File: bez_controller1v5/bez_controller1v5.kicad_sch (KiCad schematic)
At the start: 75 parts, among them J1 Conn_01x03_Male, J10 IMU Conn_01x03_Female, J11 Conn_01x03_Male, J12 Conn_01x03_Male, J13 USB_B_Mini, J2 Conn_01x03_Male, J3 Conn_01x03_Male, J4 Screw_Terminal_01x02, J5 Conn_01x03_Male, J6 Conn_01x03_Male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

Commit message: fixing some routing and components footprint
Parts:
- D2, D4: footprint LED_THT:LED_D5.0mm_Clear -> LED_SMD:LED_0603_1608Metric
- FB1, FB2: footprint Inductor_THT:L_Axial_L5.3mm_D2.2mm_P7.62mm_Horizontal_Vishay_IM-1 -> Inductor_SMD:L_0603_1608Metric
- R3: footprint Resistor_SMD:R_0603_1608Metric -> Resistor_SMD:R_0805_2012Metric
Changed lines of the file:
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@@
       (effects (font (size 1.27 1.27)) (justify right))
     )
-    (property "Footprint" "Inductor_THT:L_Axial_L5.3mm_D2.2mm_P7.62mm_Horizontal_Vishay_IM-1" (at 22.098 46.355 90)
+    (property "Footprint" "Inductor_SMD:L_0603_1608Metric" (at 22.098 46.355 90)
       (effects (font (size 1.27 1.27)) hide)
     )
@@
       (effects (font (size 1.27 1.27)))
     )
-    (property "Footprint" "Inductor_THT:L_Axial_L5.3mm_D2.2mm_P7.62mm_Horizontal_Vishay_IM-1" (at 168.275 90.678 90)
+    (property "Footprint" "Inductor_SMD:L_0603_1608Metric" (at 168.275 90.678 90)
       (effects (font (size 1.27 1.27)) hide)
     )
@@
       (effects (font (size 1.27 1.27)) (justify left))
     )
-    (property "Footprint" "Resistor_SMD:R_0603_1608Metric" (at 83.058 67.945 90)
+    (property "Footprint" "Resistor_SMD:R_0805_2012Metric" (at 83.058 67.945 90)
       (effects (font (size 1.27 1.27)) hide)
     )
@@
       (effects (font (size 1.27 1.27)) (justify right))
     )
-    (property "Footprint" "LED_THT:LED_D5.0mm_Clear" (at 109.855 34.925 0)
+    (property "Footprint" "LED_SMD:LED_0603_1608Metric" (at 109.855 34.925 0)
       (effects (font (size 1.27 1.27)) hide)
     )
@@
       (effects (font (size 1.27 1.27)))
     )
-    (property "Footprint" "LED_THT:LED_D5.0mm_Clear" (at 166.37 142.24 0)
-      (effects (font (size 1.27 1.27)) hide)
-    )
+    (property "Footprint" "LED_SMD:LED_0603_1608Metric" (at 166.37 142.24 0)
+      (effects (font (size 1.27 1.27)) hide)
+    )

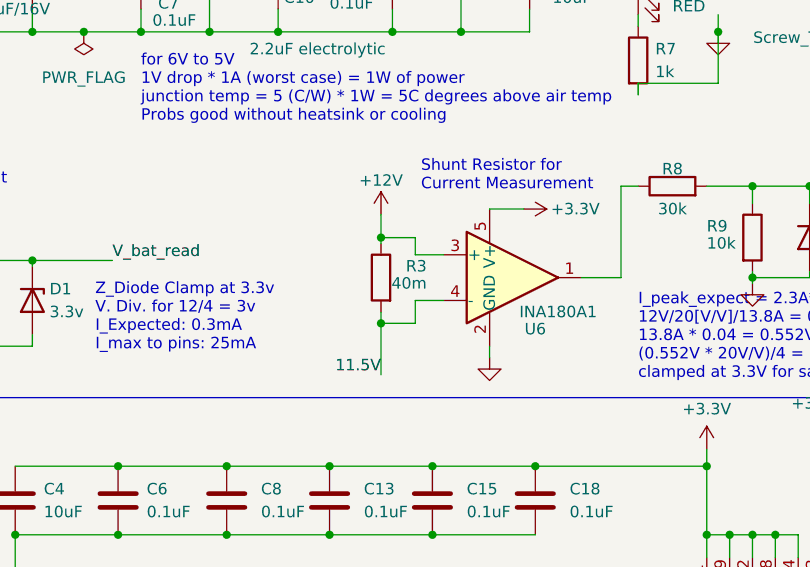
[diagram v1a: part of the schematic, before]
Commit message: change footprint of shunt R and electrolytic C
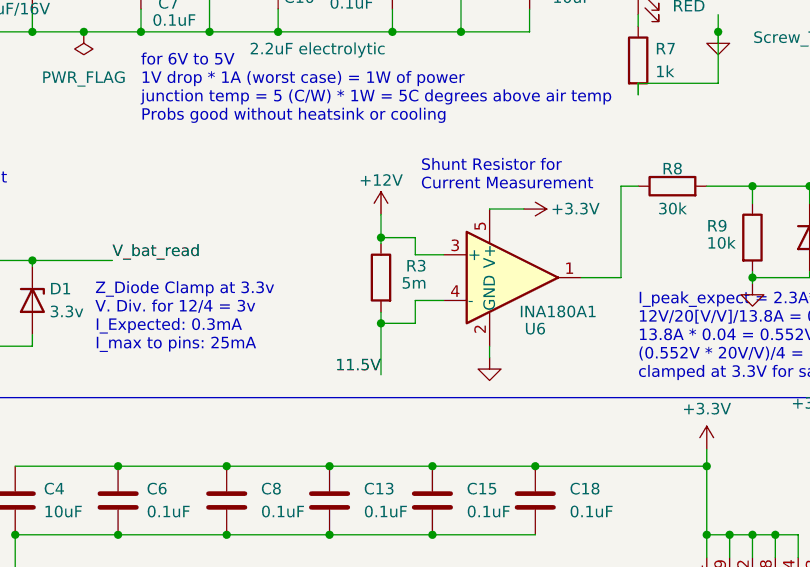
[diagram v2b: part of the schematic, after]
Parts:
- C10: footprint Capacitor_SMD:CP_Elec_4x5.4 -> Capacitor_THT:CP_Radial_D8.0mm_P3.50mm
- R3: value 40m -> 5m; footprint Resistor_SMD:R_0805_2012Metric -> Resistor_SMD:R_2010_5025Metric
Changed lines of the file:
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@@
       (effects (font (size 1.27 1.27)) (justify left))
     )
-    (property "Value" "40m" (at 86.36 68.58 0)
-      (effects (font (size 1.27 1.27)) (justify left))
-    )
-    (property "Footprint" "Resistor_SMD:R_0805_2012Metric" (at 83.058 67.945 90)
+    (property "Value" "5m" (at 86.36 68.58 0)
+      (effects (font (size 1.27 1.27)) (justify left))
+    )
+    (property "Footprint" "Resistor_SMD:R_2010_5025Metric" (at 83.058 67.945 90)
       (effects (font (size 1.27 1.27)) hide)
     )
@@
       (effects (font (size 1.27 1.27)) (justify left))
     )
-    (property "Footprint" "Capacitor_SMD:CP_Elec_4x5.4" (at 70.8152 38.1 0)
-      (effects (font (size 1.27 1.27)) hide)
-    )
+    (property "Footprint" "Capacitor_THT:CP_Radial_D8.0mm_P3.50mm" (at 70.8152 38.1 0)
+      (effects (font (size 1.27 1.27)) hide)
+    )

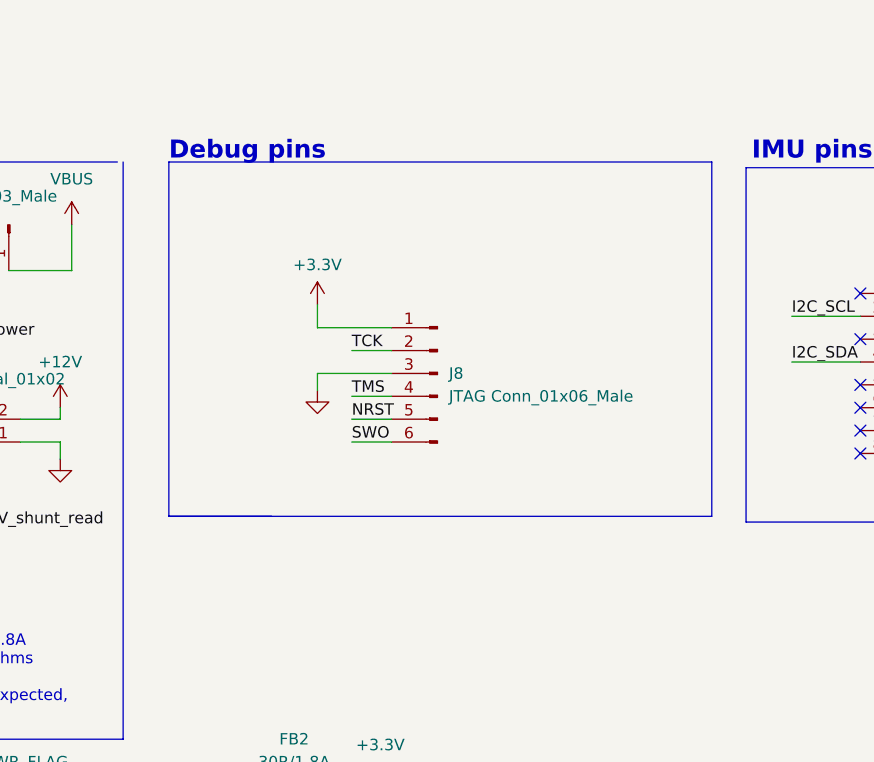
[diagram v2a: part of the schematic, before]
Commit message: add headers for GPIO/buttons
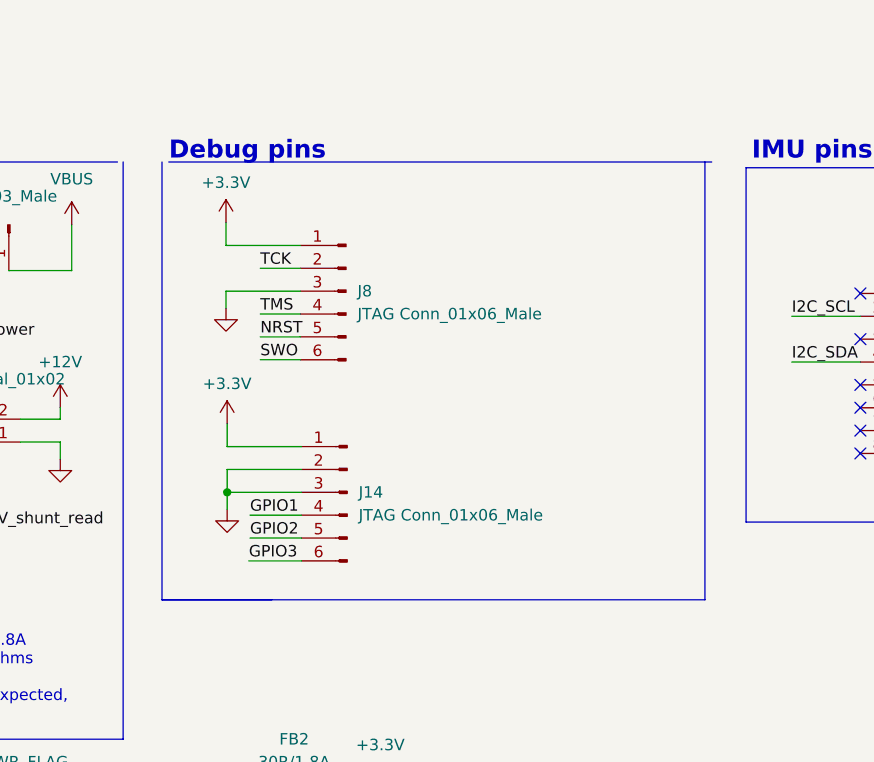
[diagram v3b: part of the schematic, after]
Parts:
- added J14: JTAG Conn_01x06_Male, Connector_PinHeader_2.54mm:PinHeader_1x06_P2.54mm_Vertical, symbol Connector:Conn_01x06_Male
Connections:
- net +3.3V: now also J14.1 (Pin_1)
- net GND: now also J14.2 (Pin_2), J14.3 (Pin_3)
- new net GPIO1: J14.4 (Pin_4)
- new net GPIO2: J14.5 (Pin_5)
- new net GPIO3: J14.6 (Pin_6)
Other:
- moved on the sheet: J8

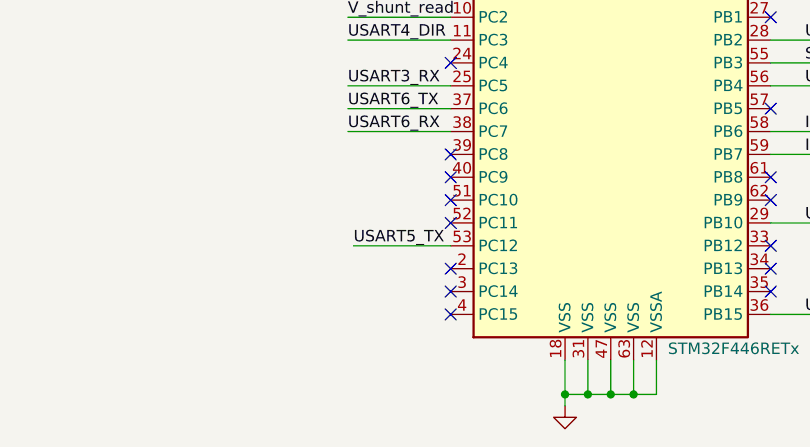
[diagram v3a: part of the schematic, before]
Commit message: routed IMU pins and minor changes
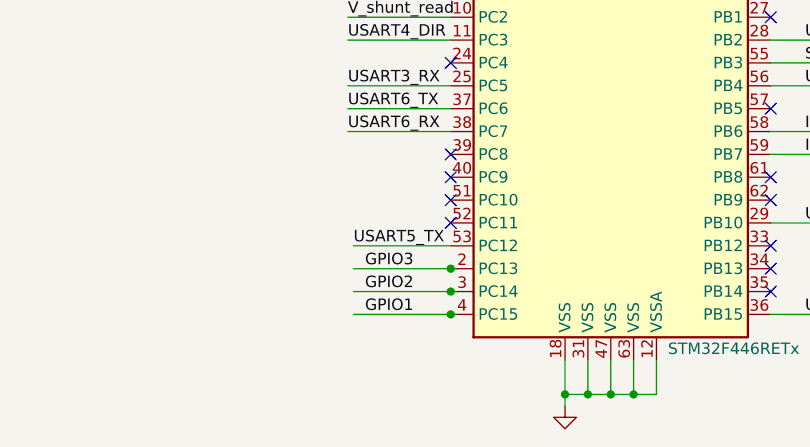
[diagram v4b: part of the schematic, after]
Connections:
- net GPIO1: now also U7.4 (PC15)
- net GPIO2: now also U7.3 (PC14)
- net GPIO3: now also U7.2 (PC13)
- no-connect marks 29 -> 26
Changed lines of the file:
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@@
   (junction (at 52.07 88.9) (diameter 0) (color 0 0 0 0)
   )
+  (junction (at 104.775 182.88) (diameter 0) (color 0 0 0 0)
+  )
   (junction (at 64.135 88.9) (diameter 0) (color 0 0 0 0)
   )
@@
   )
   (junction (at 133.35 -45.085) (diameter 0) (color 0 0 0 0)
+  )
+  (junction (at 104.775 180.34) (diameter 0) (color 0 0 0 0)
+  )
+  (junction (at 104.775 177.8) (diameter 0) (color 0 0 0 0)
   )
   (junction (at 81.28 73.025) (diameter 0) (color 0 0 0 0)
@@
   (no_connect (at 104.775 167.64))
   (no_connect (at 140.335 160.02))
-  (no_connect (at 104.775 180.34))
   (no_connect (at 104.775 165.1))
   (no_connect (at 140.335 177.8))
-  (no_connect (at 104.775 177.8))
   (no_connect (at 140.335 149.86))
   (no_connect (at 276.86 135.255))
@@
   (no_connect (at 140.335 147.32))
   (no_connect (at 231.14 31.75))
-  (no_connect (at 104.775 182.88))
   (no_connect (at 231.14 44.45))
   (no_connect (at 104.775 144.78))
@@
     (stroke (width 0) (type default))
   )
+  (wire (pts (xy 93.98 182.88) (xy 104.775 182.88))
+    (stroke (width 0) (type default))
+  )
   (wire (pts (xy 143.51 24.13) (xy 143.51 29.21))
     (stroke (width 0) (type default))
@@
     (stroke (width 0) (type default))
   )
+  (wire (pts (xy 93.98 180.34) (xy 104.775 180.34))
+    (stroke (width 0) (type default))
+  )
   (polyline (pts (xy 283.21 90.805) (xy 283.21 73.66))
     (stroke (width 0) (type default))
@@
     (stroke (width 0) (type default))
   )
+  (wire (pts (xy 104.775 177.8) (xy 105.41 177.8))
+    (stroke (width 0) (type default))
+  )
   (wire (pts (xy 54.61 40.64) (xy 62.23 40.64))
     (stroke (width 0) (type default))
@@
     (stroke (width 0) (type default))
   )
+  (wire (pts (xy 93.98 177.8) (xy 104.775 177.8))
+    (stroke (width 0) (type default))
+  )
   (wire (pts (xy 62.23 36.83) (xy 62.23 40.64))
     (stroke (width 0) (type default))
@@
     (stroke (width 0) (type default))
   )
+  (wire (pts (xy 104.775 182.88) (xy 105.41 182.88))
+    (stroke (width 0) (type default))
+  )
   (wire (pts (xy 164.465 39.116) (xy 168.91 39.116))
     (stroke (width 0) (type default))
@@
   )
   (wire (pts (xy 52.07 96.52) (xy 64.135 96.52))
+    (stroke (width 0) (type default))
+  )
+  (wire (pts (xy 104.775 180.34) (xy 105.41 180.34))
     (stroke (width 0) (type default))
   )
@@
     (effects (font (size 1.27 1.27)) (justify left bottom))
   )
+  (label "GPIO2" (at 95.25 180.34 0) (fields_autoplaced)
+    (effects (font (size 1.27 1.27)) (justify left bottom))
+  )
+  (label "GPIO1" (at 95.25 182.88 0) (fields_autoplaced)
+    (effects (font (size 1.27 1.27)) (justify left bottom))
+  )
   (label "NRST" (at 164.465 36.576 0) (fields_autoplaced)
     (effects (font (size 1.27 1.27)) (justify left bottom))
@@
     (effects (font (size 1.27 1.27)) (justify left bottom))
   )
+  (label "GPIO3" (at 95.25 177.8 0) (fields_autoplaced)
+    (effects (font (size 1.27 1.27)) (justify left bottom))
+  )

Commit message: added label for pins, changed USB and C10 footprint
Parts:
- C10: footprint Capacitor_THT:CP_Radial_D8.0mm_P3.50mm -> Capacitor_THT:CP_Radial_D5.0mm_P2.00mm
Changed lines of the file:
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@@
       (effects (font (size 1.27 1.27)) (justify left))
     )
-    (property "Footprint" "Capacitor_THT:CP_Radial_D8.0mm_P3.50mm" (at 70.8152 38.1 0)
+    (property "Footprint" "Capacitor_THT:CP_Radial_D5.0mm_P2.00mm" (at 70.8152 38.1 0)
       (effects (font (size 1.27 1.27)) hide)
     )

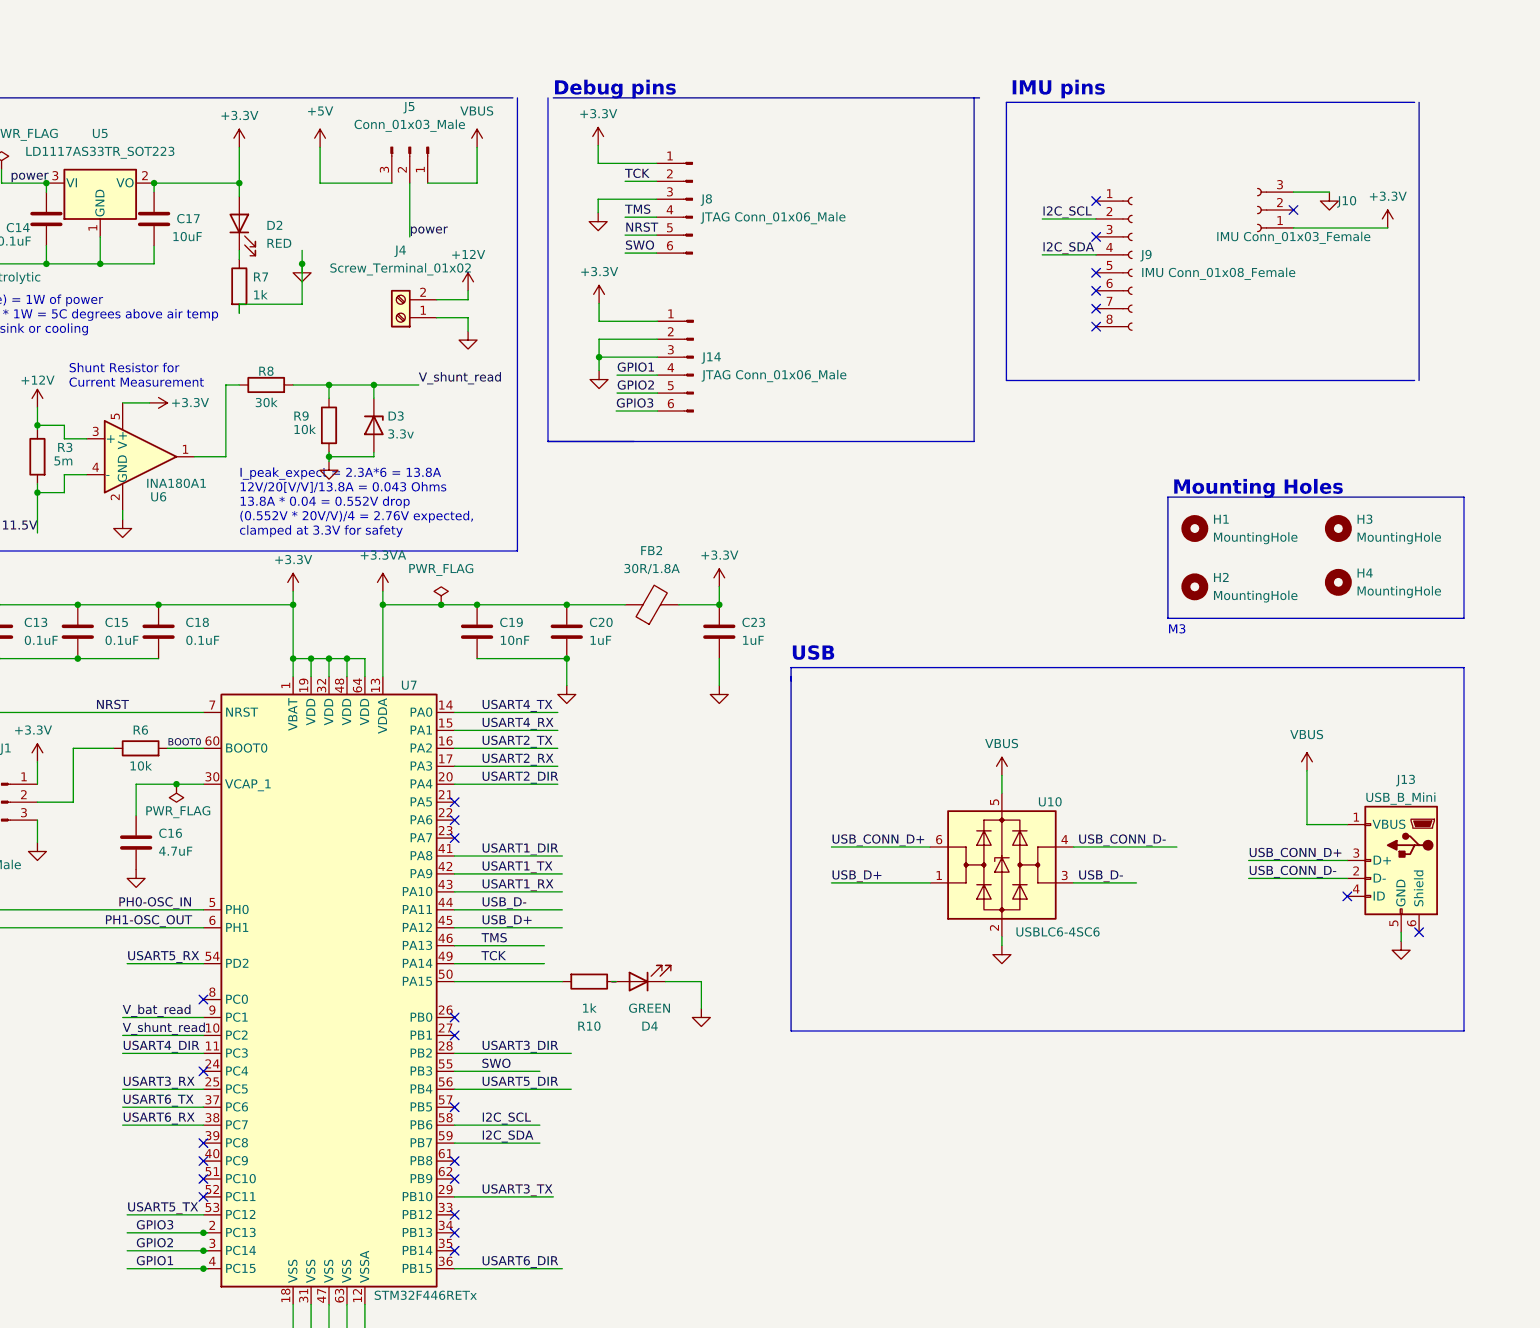
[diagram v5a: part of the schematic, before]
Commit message: Add SPI lines for IMU
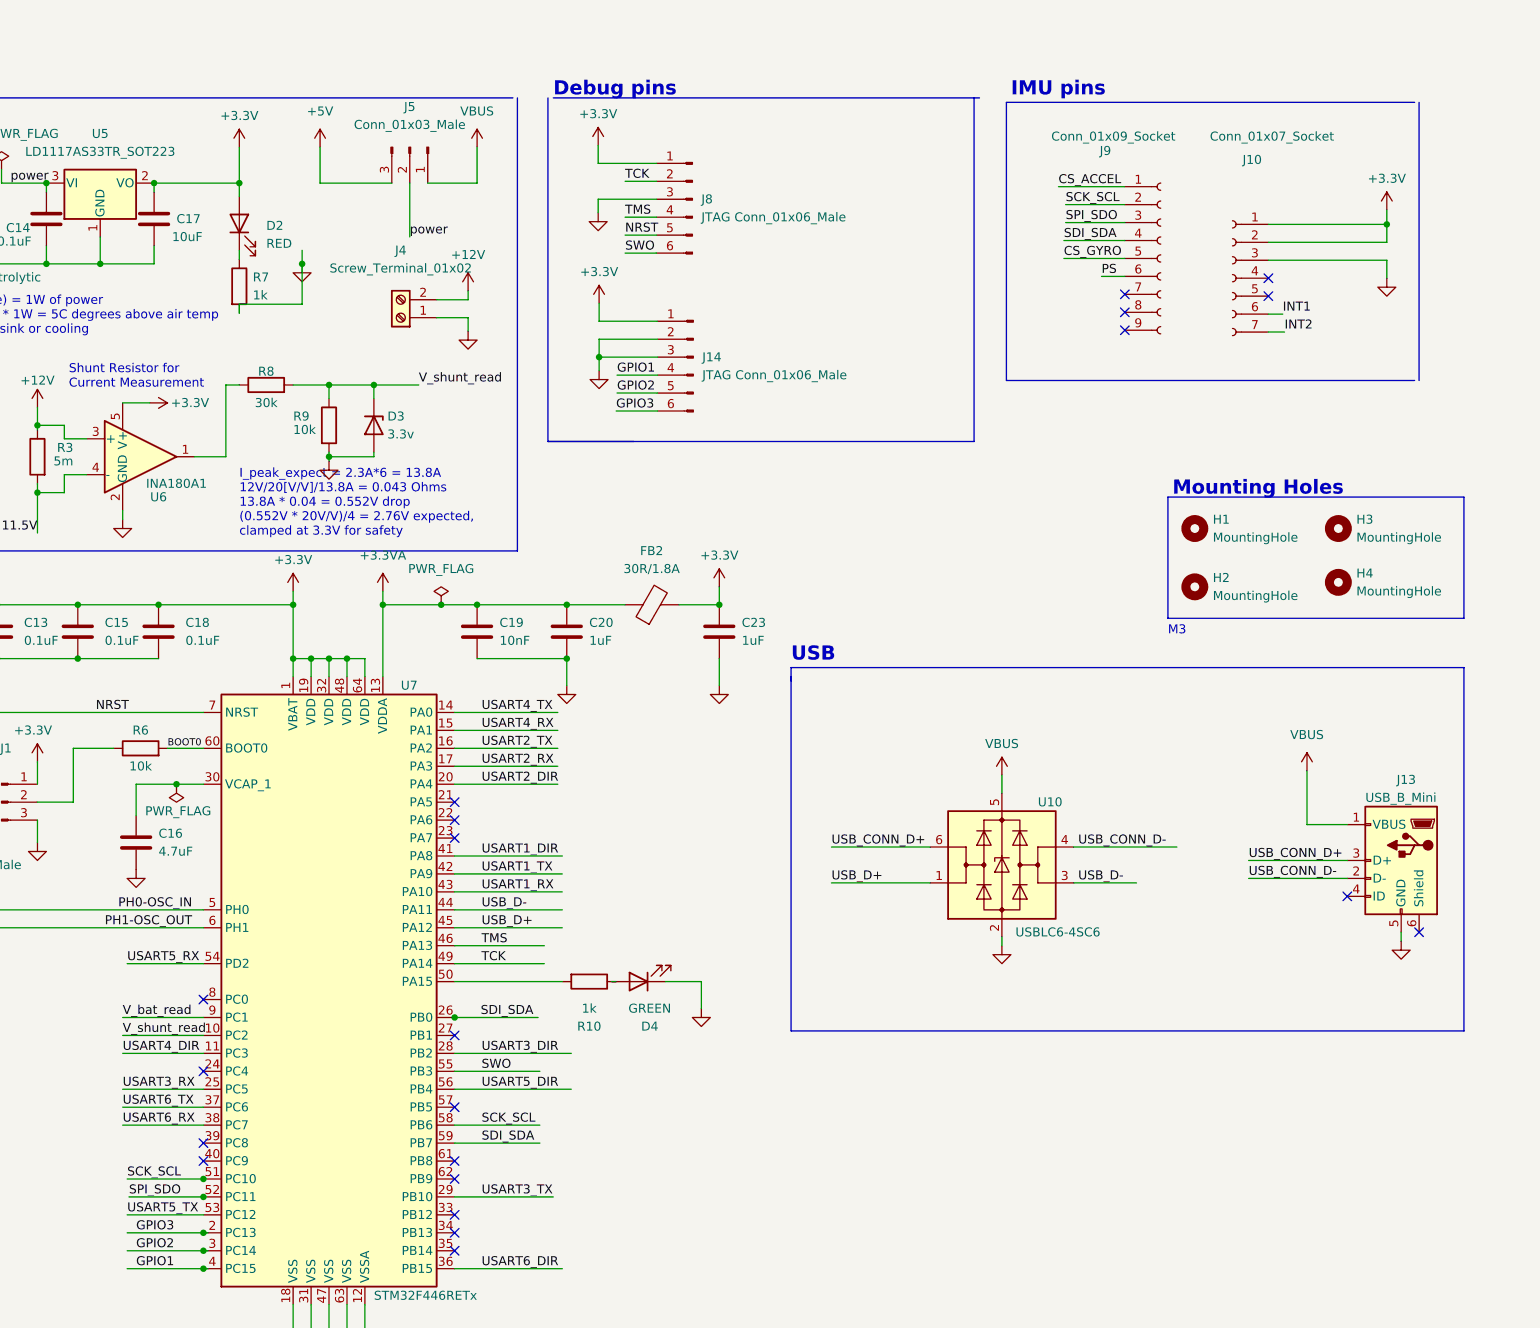
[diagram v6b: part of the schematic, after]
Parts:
- removed J10: IMU Conn_01x03_Female, Connector_PinSocket_1.27mm:PinSocket_1x03_P1.27mm_Vertical, symbol Connector:Conn_01x08_Female
- removed J9: IMU Conn_01x08_Female, Connector_PinSocket_1.27mm:PinSocket_1x08_P1.27mm_Vertical, symbol Connector:Conn_01x08_Female
- added J10: Conn_01x07_Socket, Connector_PinSocket_1.27mm:PinSocket_1x07_P1.27mm_Vertical, symbol Connector:Conn_01x07_Socket
- added J9: Conn_01x09_Socket, Connector_PinSocket_1.27mm:PinSocket_1x09_P1.27mm_Vertical, symbol Connector:Conn_01x09_Socket
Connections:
- net I2C_SCL is gone; now on net SCK_SCL: U7.58 (PB6)
- net I2C_SDA is gone; now on net SDI_SDA: U7.59 (PB7)
- net +3.3V: now also J10.1 (Pin_1), J10.2 (Pin_2)
- net GND: now also J10.3 (Pin_3)
- net SDI_SDA: now reaches U7.26 (PB0)
- net SDI_SDA: now also J9.4 (Pin_4)
- net SCK_SCL: now reaches U7.51 (PC10)
- net SCK_SCL: now also J9.2 (Pin_2)
- net SPI_SDO: now reaches U7.52 (PC11)
- net SPI_SDO: now also J9.3 (Pin_3)
- new net CS_ACCEL: J9.1 (Pin_1)
- new net CS_GYRO: J9.5 (Pin_5)
- new net INT1: J10.6 (Pin_6)
- new net INT2: J10.7 (Pin_7)
- new net PS: J9.6 (Pin_6)
- no-connect marks 26 -> 21
